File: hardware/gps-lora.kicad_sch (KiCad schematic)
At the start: 0 parts

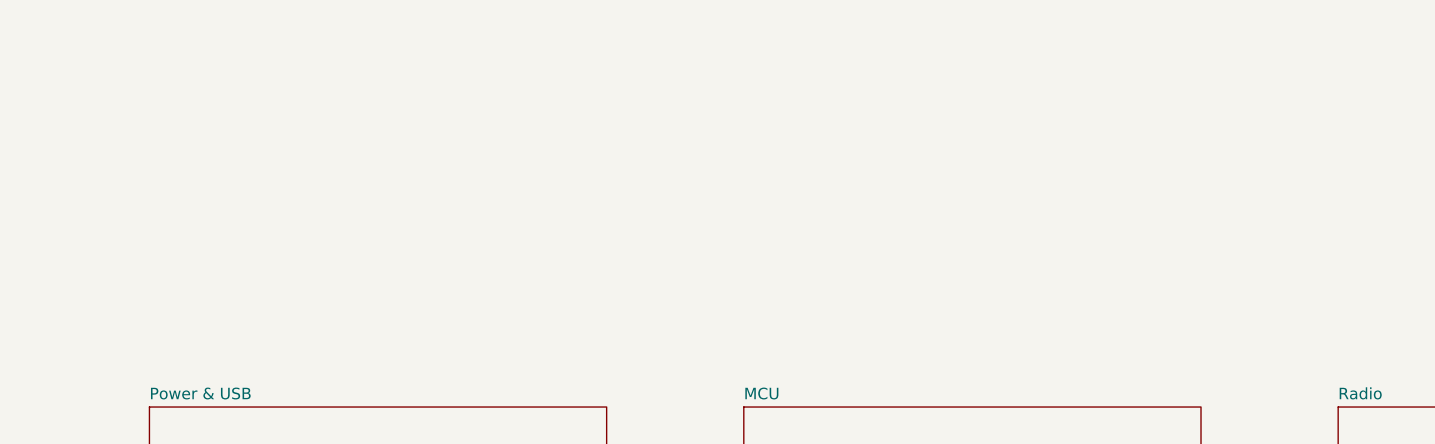
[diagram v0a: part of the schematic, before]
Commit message: Complete schematic, place and partially route the PCB
Schematic:
- Add Storage & Display sheet (microSD, FH12 OLED connector, TLV75801
  3.8 V VBAT regulator, charge-pump parts) and Radio sheet fixes
- Select remaining parts (PTS810, 1206L075THYR, SMF5.0A, MCP120 EN
  supervisor DNP, Elna DSK backup cap), add mounting holes and fiducials
- Pin changes for routability: PPS -> IO15, LoRa MOSI -> IO47,
  LoRa RESET -> IO48, LoRa DIO0 -> IO1
- Remove optional SPI clock filter parts (R309/C307, R310/C308)
- Remove company name from title blocks (personal project)

PCB (60 x 120 mm, 4 layers):
- Place all parts; GNSS zone with custom DRC rules (kicad_dru)
- Project ESP32-S3-WROOM-1 footprint with 0.4 mm thermal vias
- GND / +3V3 / +5V copper zones
- Route power path, GNSS, microSD and LoRa buses
- DRC clean except unrouted nets and expected silkscreen-at-edge items

Docs: selected-parts table, pin table and EMC deviation in PCB_DESIGN.md

Co-Authored-By: Claude Opus 5.5 <noreply@anthropic.com>
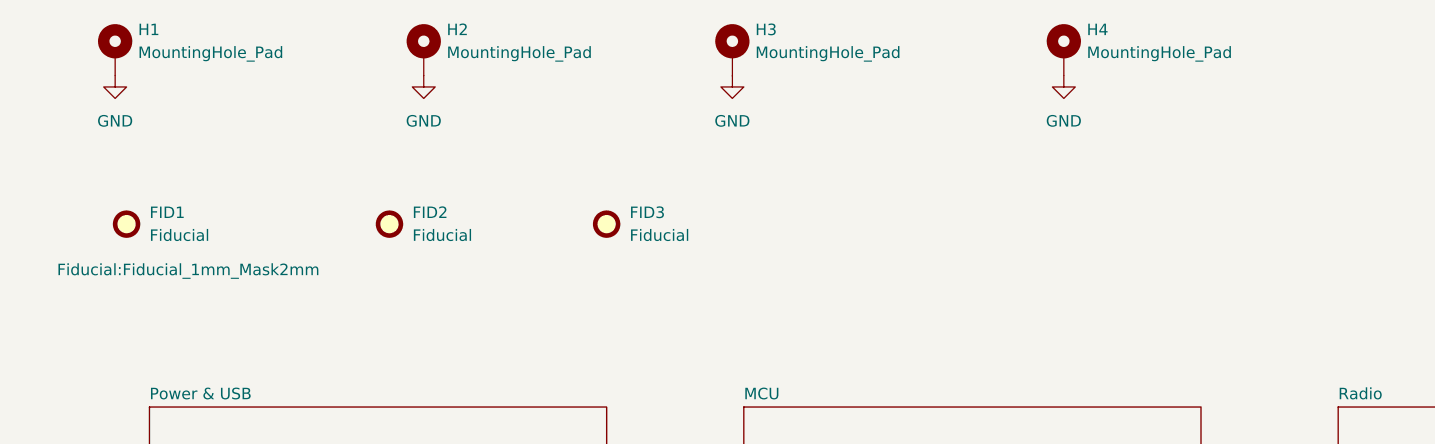
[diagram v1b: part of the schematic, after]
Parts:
- added FID1, FID2, FID3: Fiducial, Fiducial:Fiducial_1mm_Mask2mm, symbol Mechanical:Fiducial
- added H1, H2, H3, H4: MountingHole_Pad, MountingHole:MountingHole_2.2mm_M2_Pad_Via, symbol Mechanical:MountingHole_Pad
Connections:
- new net GND: H1.1, H2.1, H3.1, H4.1
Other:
- company: SSS-Defence -> (none)
